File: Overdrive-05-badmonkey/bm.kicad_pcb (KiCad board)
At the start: 2 copper layers, 62 x 40 mm, 37 parts, among them J1 Conn_01x04_Pin, Q1 2N3904, U1 4558, U2 4558

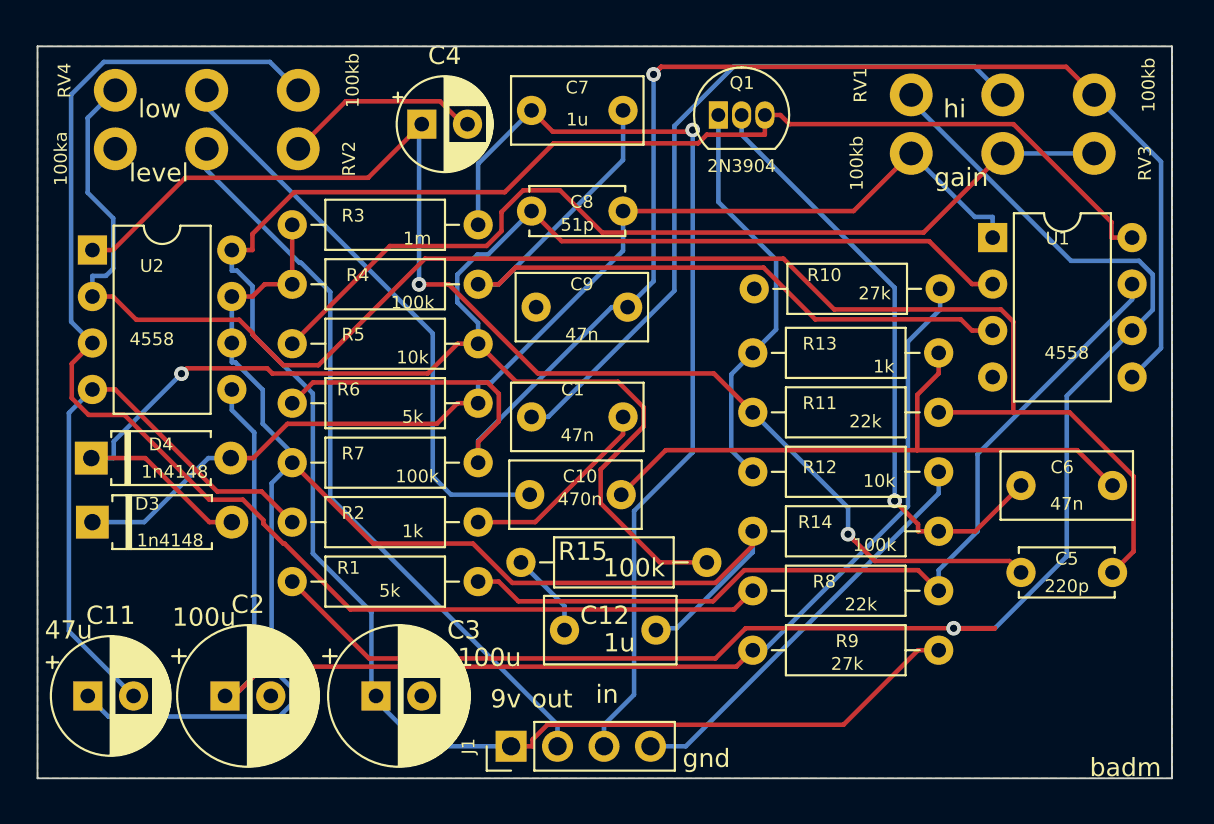
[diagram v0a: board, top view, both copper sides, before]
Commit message: re-generated the Fatdrive and badmonkey boards, as they were just a hair too large for the enclosures I am using.
x
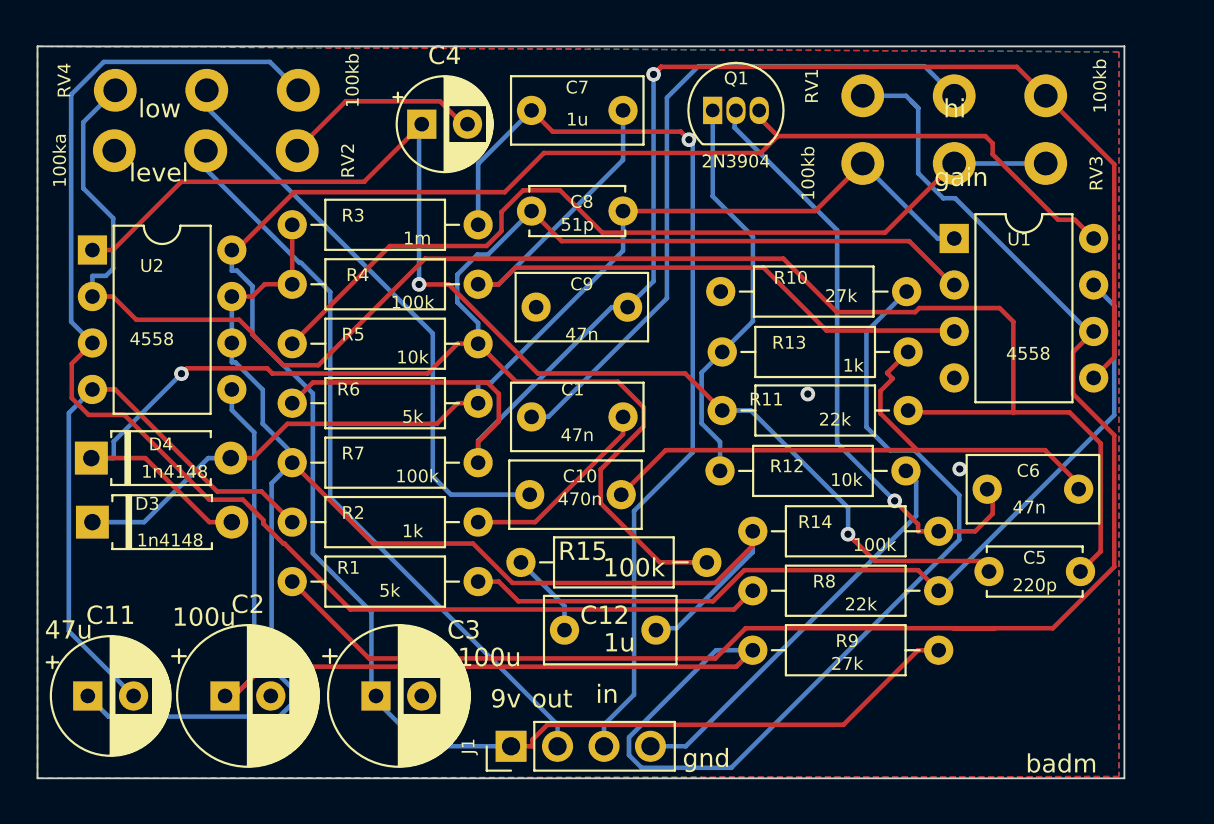
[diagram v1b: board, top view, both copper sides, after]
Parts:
- moved RV3 2.71 mm to (145.1, 106.4)
- moved RV1 2.65 mm to (155.1, 102.7)
- moved U1 2.10 mm to (150.1, 110.5)
- moved C6 1.86 mm to (151.9, 124.2)
- moved R10 1.84 mm to (137.3, 113.4)
- moved R12 1.79 mm to (137.3, 123.2)
- moved C5 1.75 mm to (157.0, 128.7)
- moved R11 1.67 mm to (137.4, 119.9)
- moved R13 1.67 mm to (137.4, 116.7)
- moved Q1 0.40 mm to (136.9, 103.5)
- moved RV2 0.11 mm to (104.2, 105.7)
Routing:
- net Net-(U2B-+): track 70.7 -> 97.0 mm
- net Net-(U1B--): track 90.2 -> 85.8 mm, vias 1 -> 0
- net Net-(U1B-+): track 86.8 -> 83.9 mm
- net +9V: track 118.9 -> 116.4 mm
- net Net-(D3-K): track 62.0 -> 59.6 mm
- net Net-(D3-A): track 94.1 -> 91.9 mm
- net Net-(C4-Pad1): track 71.9 -> 69.8 mm
- net Net-(R5-Pad1): track 50.7 -> 48.6 mm
- net Net-(U1A-+): track 43.4 -> 41.3 mm
- net Net-(C1-Pad1): track 39.6 -> 38.1 mm
- net Net-(U2A--): track 91.9 -> 93.2 mm
- net IN: track 52.8 -> 52.3 mm
- net GND: track 56.1 -> 55.6 mm, vias 0 -> 2
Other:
- board size 62 x 40 mm -> 59.4 x 40 mm
- board text added: "125b-59x40"
- board text removed: "125b-62x40"
